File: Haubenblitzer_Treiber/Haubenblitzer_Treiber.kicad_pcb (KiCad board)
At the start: 2 copper layers, 75 x 60 mm, 39 parts, among them J1 ISCP, J2 Micro_USB, J3 Screw_Terminal_01x02, J4 Screw_Terminal_01x03, J5 Screw_Terminal_01x05, J6 RJ12, J7 RJ12, Q1 MMBT3906, Q2 MMBT3906, U1 ATmega32U4-AU, U2 NCV8460, U3 3021-D-E-1000, U4 3021-D-E-1000, Y1 Crystal

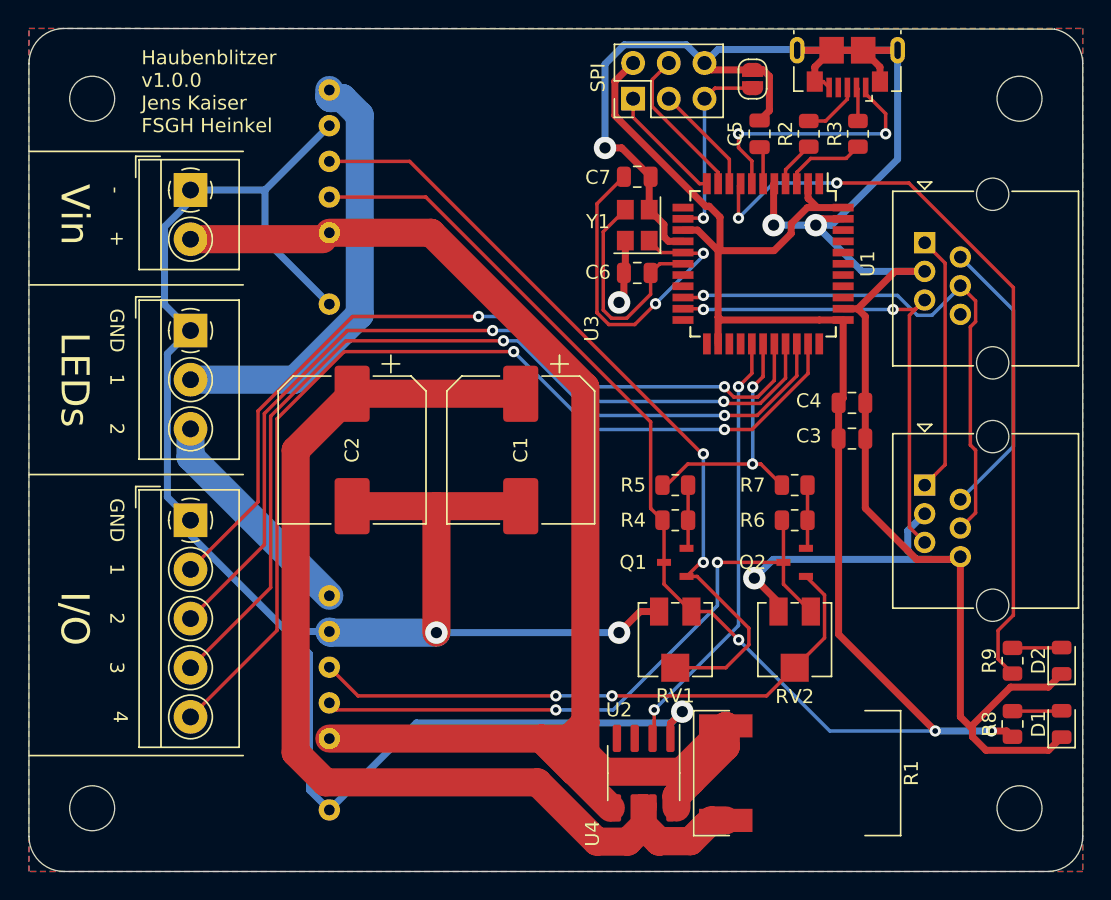
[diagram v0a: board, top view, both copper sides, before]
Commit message: added ESD protection and gerber files
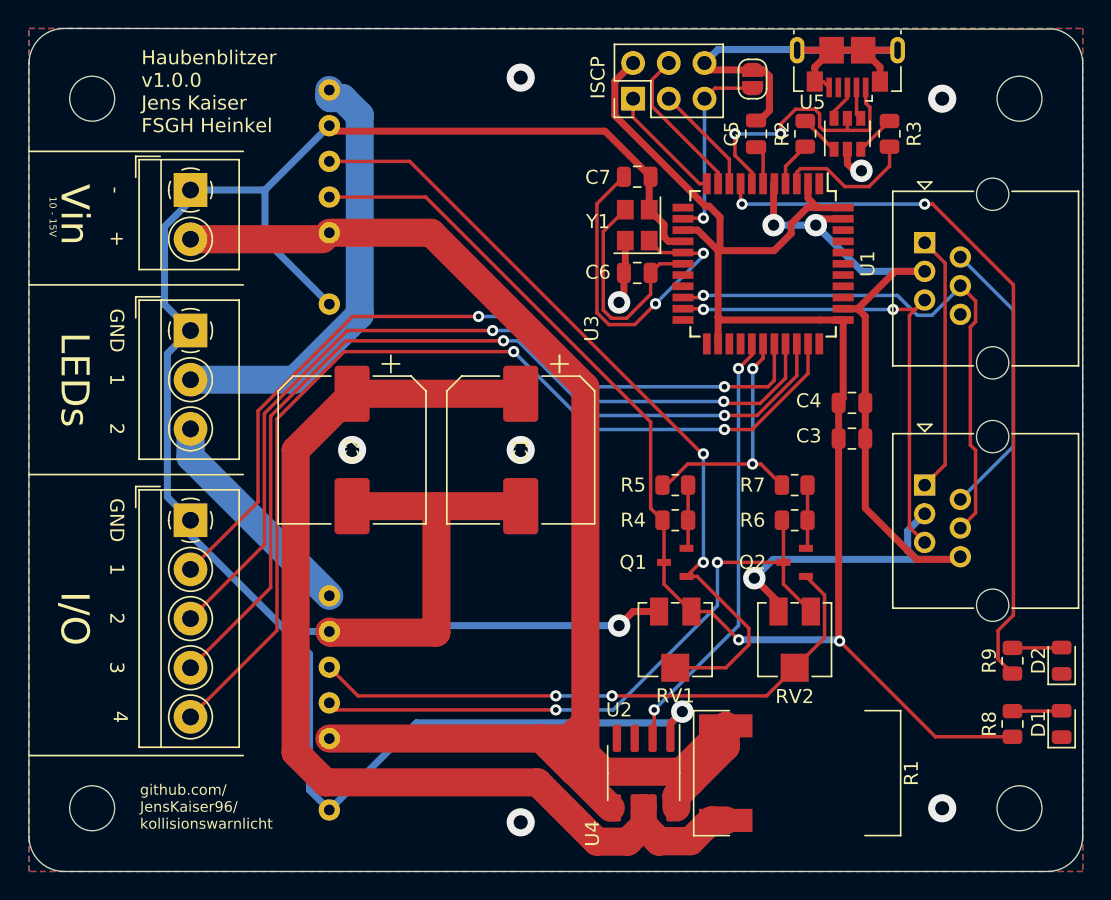
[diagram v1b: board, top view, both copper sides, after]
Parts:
- added U5: USBLC6-2P6, Package_TO_SOT_SMD:SOT-23-6, F.Cu at (78.2, 137.5)
- moved R3 2.25 mm to (81.2, 137.5), turned to 270 degrees
- moved C5 0.25 mm to (71.8, 137.5)
- moved R2 0.25 mm to (75.2, 137.5)
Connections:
- net Net-(J6-Pad1) renamed RJ12_V1
- net Net-(J6-Pad2) renamed RJ12_V2
- R2 pad 2: Net-(J2-Pad3) -> Net-(R2-Pad2)
- R3 pad 1: D- -> Net-(R3-Pad1)
- R3 pad 2: Net-(J2-Pad2) -> D-
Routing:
- net GND: track 331.1 -> 303.1 mm, vias 8 -> 13
- net LED1_Ref: track 151.4 -> 142.2 mm, vias 3 -> 2
- net D-: track 5.92 -> 10.0 mm
- net Net-(R3-Pad1): track 0.00 -> 2.88 mm
- net Net-(R2-Pad2): track 0.00 -> 2.88 mm
- net RX_LED: track 54.5 -> 51.7 mm
- net U_bus: track 18.3 -> 19.9 mm
- net Net-(J2-Pad3): track 4.23 -> 2.59 mm
- net IO_misc1: track 58.3 -> 57.7 mm
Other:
- board text added: "10 - 15V"
- board text added: "ISCP"
- board text added: "github.com/ JensKaiser96/ kollisionswarnlicht"
- board text removed: "SPI"

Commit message: Version2.0
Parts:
- removed D1, D2: LED, LED_SMD:LED_0805_2012Metric
- removed U5: USBLC6-2P6, Package_TO_SOT_SMD:SOT-23-6
- added C8: 0.1uF, Capacitor_SMD:C_0805_2012Metric, F.Cu at (185.0, 111.0)
- added C9: 10uF, Capacitor_SMD:C_0805_2012Metric, F.Cu at (182.5, 111.0)
- added ERR: LED, LED_SMD:LED_0805_2012Metric, F.Cu at (198.0, 128.0)
- added JP2: Jumper, Jumper:SolderJumper-3_P1.3mm_Open_RoundedPad1.0x1.5mm, B.Cu at (178.5, 126.2)
- added JP3: Jumper, Jumper:SolderJumper-3_P1.3mm_Open_RoundedPad1.0x1.5mm, B.Cu at (178.5, 138.2)
- added JP4: Jumper, Jumper:SolderJumper-2_P1.3mm_Open_RoundedPad1.0x1.5mm, B.Cu at (181.5, 126.9)
- added JP5: Jumper, Jumper:SolderJumper-2_P1.3mm_Open_RoundedPad1.0x1.5mm, B.Cu at (181.5, 138.9)
- added JP6: Jumper, Jumper:SolderJumper-2_P1.3mm_Open_Pad2.0x4.0mm, B.Cu at (135.2, 108.2)
- added PWR: LED, LED_SMD:LED_0805_2012Metric, F.Cu at (198.0, 132.0)
- added Q3: AO3401A, Package_TO_SOT_SMD:SOT-23, F.Cu at (174.5, 126.8)
- added Q4: AO3401A, Package_TO_SOT_SMD:SOT-23, F.Cu at (174.5, 138.8)
- added R10: 1K, Resistor_SMD:R_0805_2012Metric, F.Cu at (179.0, 132.8)
- added R11: 5K, Resistor_SMD:R_0805_2012Metric, F.Cu at (179.0, 135.2)
- added R12: 5k, Resistor_SMD:R_0805_2012Metric, F.Cu at (174.5, 135.2)
- added R13: 220, Resistor_SMD:R_0805_2012Metric, F.Cu at (195.5, 128.0)
- added R14: 5.1K, Resistor_SMD:R_0805_2012Metric, F.Cu at (185.0, 94.0)
- added R15: 22, Resistor_SMD:R_0805_2012Metric, F.Cu at (180.0, 94.0)
- added R16: 22, Resistor_SMD:R_0805_2012Metric, F.Cu at (182.5, 94.0)
- added R17: 5.1K, Resistor_SMD:R_0805_2012Metric, F.Cu at (177.5, 94.0)
- C1: value 220uF -> 1uF; footprint Capacitor_SMD:CP_Elec_10x10 -> Capacitor_SMD:C_0805_2012Metric
- C2: value 220uF -> 4.7uF; footprint Capacitor_SMD:CP_Elec_10x10 -> Capacitor_SMD:C_0805_2012Metric
- C3: value 0.1uF -> 220uF; footprint Capacitor_SMD:C_0805_2012Metric -> Capacitor_SMD:CP_Elec_10x10
- C4: value 10uF -> 220uF; footprint Capacitor_SMD:C_0805_2012Metric -> Capacitor_SMD:CP_Elec_10x10
- C5: value 1uF -> 18pF
- C7: value 18pF -> 1uF
- J1: value ISCP -> Screw_Terminal; footprint Connector_PinHeader_2.54mm:PinHeader_2x03_P2.54mm_Vertical -> TerminalBlock_4Ucon:TerminalBlock_4Ucon_1x02_P3.50mm_Horizontal
- J2: value Micro_USB -> Screw_Terminal; footprint Connector_USB:USB_Micro-B_GCT_USB3076-30-A -> TerminalBlock_4Ucon:TerminalBlock_4Ucon_1x03_P3.50mm_Horizontal
- J3: value Screw_Terminal_01x02 -> ISCP; footprint TerminalBlock_4Ucon:TerminalBlock_4Ucon_1x02_P3.50mm_Horizontal -> Connector_PinHeader_2.54mm:PinHeader_2x03_P2.54mm_Vertical
- J4: value Screw_Terminal_01x03 -> Screw_Terminal; footprint TerminalBlock_4Ucon:TerminalBlock_4Ucon_1x03_P3.50mm_Horizontal -> TerminalBlock_4Ucon:TerminalBlock_4Ucon_1x05_P3.50mm_Horizontal
- J5: value Screw_Terminal_01x05 -> RJ12; footprint TerminalBlock_4Ucon:TerminalBlock_4Ucon_1x05_P3.50mm_Horizontal -> Connector_RJ:RJ25_Wayconn_MJEA-660X1_Horizontal
- J7: value RJ12 -> USB_C_4510; footprint Connector_RJ:RJ25_Wayconn_MJEA-660X1_Horizontal -> Connector_USB:USB_C_4510
- JP1: value Reset -> Jumper; footprint Jumper:SolderJumper-2_P1.3mm_Open_RoundedPad1.0x1.5mm -> Jumper:SolderJumper-2_P1.3mm_Open_Pad2.0x4.0mm; moved to B.Cu
- Q1, Q2: value MMBT3906 -> IRF7205; footprint Package_TO_SOT_SMD:SA1162 -> Package_SO:SOIC-8_IRF7205
- R1: value 5 -> 10k; footprint Resistor_SMD:MP725 -> Resistor_SMD:R_0805_2012Metric
- R2: value 22 -> 220
- R3: value 22 -> 5; footprint Resistor_SMD:R_0805_2012Metric -> Package_TO_SOT_SMD:PAK-2
- R4: value 5k -> 10k
- R5, R6: value 5k -> 200
- R7: value 5k -> 5K
- R8, R9: value 220 -> 5k
- RV1, RV2: footprint Potentiometer_SMD:Potentiometer_Vishay_TS53YJ_Vertical -> Potentiometer_SMD:Potentiometer_ACP_PS10_Vertical_Hole
- U1: value ATmega32U4-AU -> LDL1117S50R; footprint Package_QFP:TQFP-44_10x10mm_P0.8mm -> Package_TO_SOT_SMD:SOT-223
- U2: value NCV8460 -> 3021-D-E-1000; footprint Package_SO:SOIC-8_3.9x4.9mm_P1.27mm -> Converter_DCDC:3021-D-E-1000
- U4: value 3021-D-E-1000 -> ATmega16U4-AU; footprint Converter_DCDC:3021-D-E-1000 -> Package_DFN_QFN:QFN-44-1EP_7x7mm_P0.5mm_EP5.2x5.2mm
- moved J5 172.1 mm to (190.0, 98.0), turned to 90 degrees
- moved U4 152.7 mm to (181.5, 102.0), turned to 270 degrees
- moved J3 147.7 mm to (169.0, 87.5), turned to 90 degrees
- moved C2 126.1 mm to (151.0, 95.0), turned to 180 degrees
- moved J7 125.0 mm to (185.0, 89.2), turned to 180 degrees
- moved C6 120.8 mm to (173.5, 98.0), turned to 180 degrees
- moved R2 120.4 mm to (195.5, 132.0), turned to 270 degrees
- moved C7 119.1 mm to (173.5, 95.5)
- moved Y1 118.1 mm to (173.5, 101.5), turned to 270 degrees
- moved H2 116.8 mm to (197.0, 87.0)
- moved R5 116.3 mm to (174.5, 120.8)
- moved H4 116.2 mm to (197.0, 139.0)
- moved R1 116.2 mm to (134.8, 85.6), turned to 90 degrees
- moved H1 115.9 mm to (130.0, 87.0)
- moved H3 115.3 mm to (130.0, 139.0)
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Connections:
- C1 pad 1: Net-(C1-Pad1) -> GND
- C1 pad 2: GND -> VCC
- C2 pad 1: Net-(C1-Pad1) -> GND
- C2 pad 2: GND -> +5V
- C3 pad 1: GND -> /U_Driver
- C3 pad 2: LED1_Ref -> GND
- C4 pad 1: GND -> /U_Driver
- C4 pad 2: LED1_Ref -> GND
- C5 pad 2: U_cap -> /CLK_1
- C6 pad 2: CLK_1 -> /CLK_2
- C7 pad 1: CLK_2 -> GND
- C7 pad 2: GND -> Net-(C7-Pad2)
- J1 pad 1: MISO -> GND
- J1 pad 2: LED1_Ref -> VCC
- J2 pad 1: U_bus -> /GND_LED
- J2 pad 2: Net-(J2-Pad2) -> /U_LED1
- J2 pad 3: Net-(J2-Pad3) -> /U_LED2
- J3 pad 1: GND -> /MISO
- J3 pad 2: +12V -> +5V
- J4 pad 2: LED1_U+ -> /IO_MISC1
- J4 pad 3: LED2_U+ -> /IO_MISC2
- J5 pad 1: GND -> /RJ12_V1
- J5 pad 2: IO_misc1 -> /RJ12_V2
- J5 pad 3: IO_misc2 -> GND
- J5 pad 4: IO_misc3 -> /RX
- J5 pad 5: IO_misc4 -> /TX
- J6 pad 1: RJ12_V1 -> /RJ12_V1
- J6 pad 2: RJ12_V2 -> /RJ12_V2
- J6 pad 4: RX -> /RX
- J6 pad 5: TX -> /TX
- JP1 pad 1: GND -> VCC
- JP1 pad 2: RESET -> /U_Driver
- Q1 pad 1: LED1_Ctrl -> /U_Driver
- Q1 pad 2: Net-(Q1-Pad2) -> /IO_BRIDGE_INRUSH_R
- Q1 pad 3: LED1_Ref -> VCC
- Q2 pad 1: LED2_Ctrl -> /U_LED1
- Q2 pad 2: Net-(Q2-Pad2) -> /IO_LED
- Q2 pad 3: LED2_Ref -> /U_Driver
- R1 pad 1: +12V -> VCC
- R1 pad 2: Net-(C1-Pad1) -> /IO_BRIDGE_INRUSH_R
- R2 pad 1: D+ -> +5V
- R3 pad 1: Net-(R3-Pad1) -> VCC
- R3 pad 2: D- -> /U_Driver
- R4 pad 1: LED1_Ref -> /U_Driver
- R4 pad 2: Net-(Q1-Pad2) -> /IO_LED
- R5 pad 1: Net-(Q1-Pad2) -> /IO_LED
- R5 pad 2: IO_LED -> Net-(Q3-Pad1)
- R6 pad 1: LED2_Ref -> /IO_LED
- R6 pad 2: Net-(Q2-Pad2) -> Net-(Q4-Pad1)
- R7 pad 1: Net-(Q2-Pad2) -> Net-(JP4-Pad2)
- R7 pad 2: IO_LED -> GND
- R8 pad 1: LED1_Ref -> Net-(JP2-Pad3)
- R8 pad 2: Net-(D1-Pad2) (its old number) -> GND
- R9 pad 1: RX_LED -> Net-(Q3-Pad1)
- R9 pad 2: Net-(D2-Pad2) -> GND
- RV1 pad 1: GND -> Net-(JP4-Pad1)
- RV1 pad 2: LED1_Ctrl -> Net-(JP2-Pad1)
- RV1 pad 3: LED1_Ref -> +5V
- RV2 pad 1: GND -> Net-(JP5-Pad1)
- RV2 pad 2: LED2_Ctrl -> Net-(JP3-Pad1)
- RV2 pad 3: LED2_Ref -> /LED2_REF
- U1 pad 1: Net-(U1-Pad1) -> GND
- U1 pad 2: LED1_Ref -> +5V
- U1 pad 3: D- -> VCC
- U1 pad 4: D+ -> (no net)
- U2 pad 1: GND -> /U_LED1
- U2 pad 2: IO_FETctrl -> GND
- U2 pad 3: Net-(U2-Pad3) -> /LED1_CTRL
- U2 pad 4: Net-(U2-Pad4) -> +5V
- U2 pad 5: +12V -> /U_Driver
- U2 pad 6: Net-(C1-Pad1) -> GND
- U3 pad 1: LED1_U+ -> /U_LED2
- U3 pad 3: LED1_Ctrl -> /LED2_CTRL
- U3 pad 4: LED1_Ref -> /LED2_REF
- U3 pad 5: +12V -> /U_Driver
- U4 pad 1: LED2_U+ -> Net-(U4-Pad1)
- U4 pad 2: GND -> +5V
- U4 pad 3: LED2_Ctrl -> /D-
- U4 pad 4: LED2_Ref -> /D+
- U4 pad 5: +12V -> GND
- U4 pad 6: GND -> Net-(C7-Pad2)
- Y1 pad 1: CLK_2 -> /CLK_2
- Y1 pad 3: CLK_1 -> /CLK_1
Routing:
- net /U_Driver: track 0.00 -> 333.6 mm, vias 0 -> 1
- net +5V: track 0.00 -> 213.2 mm, vias 0 -> 4
- net LED1_Ref: track 142.2 -> 0.00 mm, vias 2 -> 0
- net VCC: track 0.00 -> 112.3 mm, vias 0 -> 1
- net +12V: track 110.2 -> 0.00 mm
- net Net-(C1-Pad1): track 93.4 -> 0.00 mm
- net GND: track 303.1 -> 210.7 mm, vias 13 -> 17
- net /IO_MISC1: track 0.00 -> 79.3 mm, vias 0 -> 1
- net /IO_MISC2: track 0.00 -> 77.1 mm, vias 0 -> 1
- net /IO_MISC3: track 0.00 -> 74.9 mm, vias 0 -> 1
- net /IO_MISC4: track 0.00 -> 72.7 mm, vias 0 -> 1
- net /IO_LED: track 0.00 -> 72.4 mm, vias 0 -> 2
- net IO_misc4: track 69.6 -> 0.00 mm, vias 2 -> 0
- net /LED1_CTRL: track 0.00 -> 68.0 mm, vias 0 -> 4
- net IO_misc3: track 65.6 -> 0.00 mm, vias 2 -> 0
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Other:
- outline, holes or cut-outs redrawn
- board text added: "+5V"
- board text added: "- DIRECT (U1&Q2)"
- board text added: "- DRIVER (U2&U3)"
- board text added: "1+"
- board text added: "2+"
- board text added: "CTRL"
- board text added: "DRIVER MODE: I adj/max"
- board text added: "LED+"
- board text added: "LED-"
- board text added: "MISO"
- board text added: "MODES:"
- board text added: "MOSI"
- board text added: "Overcurrent Protection: ◼:OFF ◻:ON"
- board text added: "REF"
- board text added: "RST"
- board text added: "SCK"
- board text added: "Vin+"
- board text added: "Vin-"
- board text added: "adj. I LED1"
- board text added: "adj. I LED2"
- board text added: "adj:"
- board text added: "max:"
- board text added: "◼: only when set to max"
- board text removed: "-"
- board text removed: "10 - 15V"
- board text removed: "Haubenblitzer v1.0.0 Jens Kaiser FSGH Heinkel"
- board text removed: "ISCP"
- board text removed: "github.com/ JensKaiser96/ kollisionswarnlicht"
